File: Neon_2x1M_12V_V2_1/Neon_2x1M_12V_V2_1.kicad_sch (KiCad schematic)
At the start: 32 parts, among them J2 Barrel_Jack_MountingPin, J6 Conn_01x03_Pin, J7 Screw_Terminal_01x02, J8 Screw_Terminal_01x02, Q3 AO3400A, Q4 AO3400A, SW1 SW_Push, SW2 SW_Push, U1 ESP32-WROOM-32, U2 AMS1117-3.3

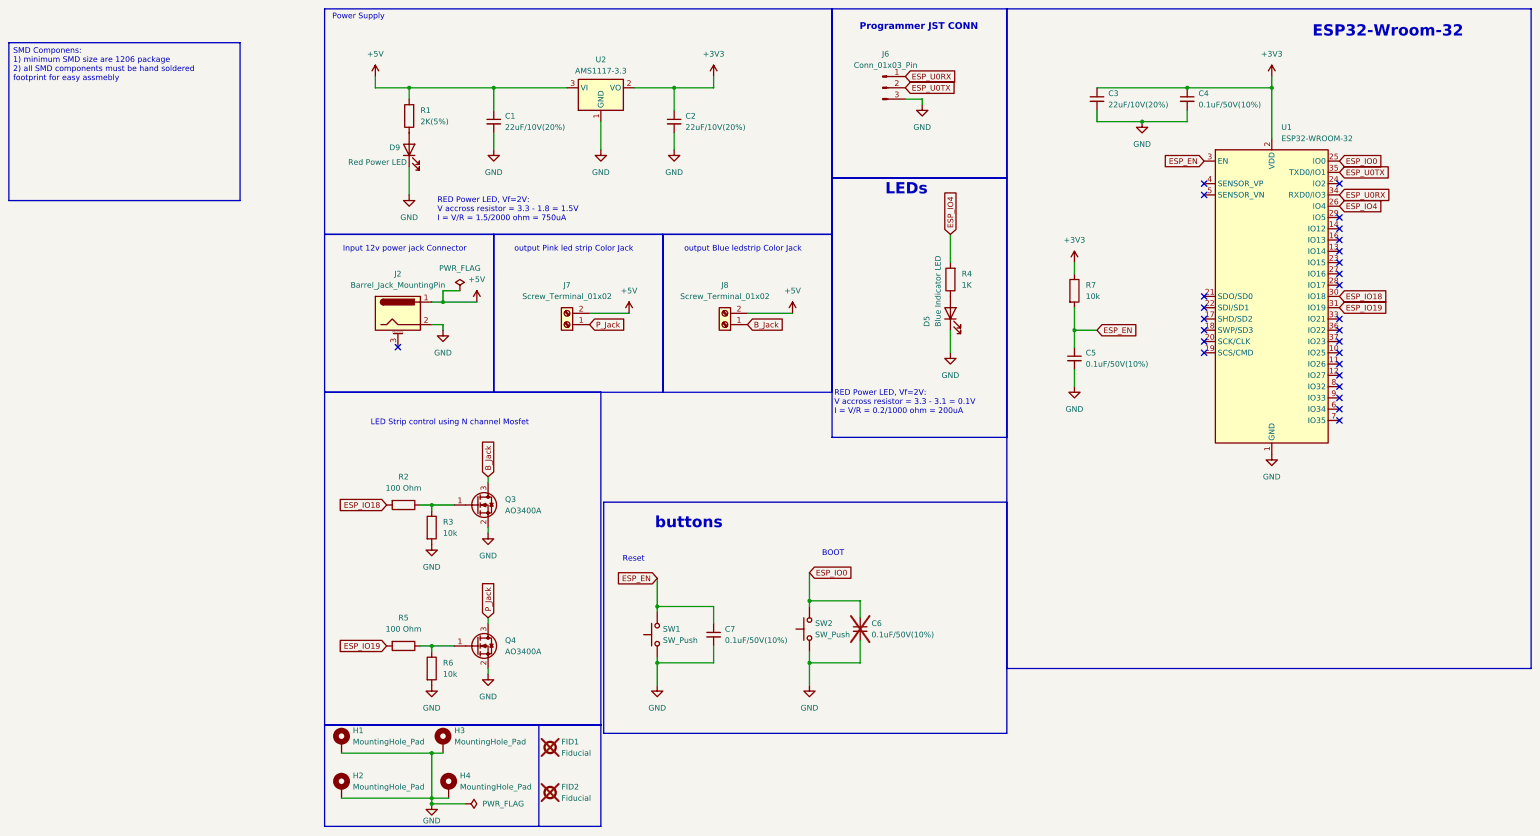
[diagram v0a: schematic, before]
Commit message: updated schematic and footprints
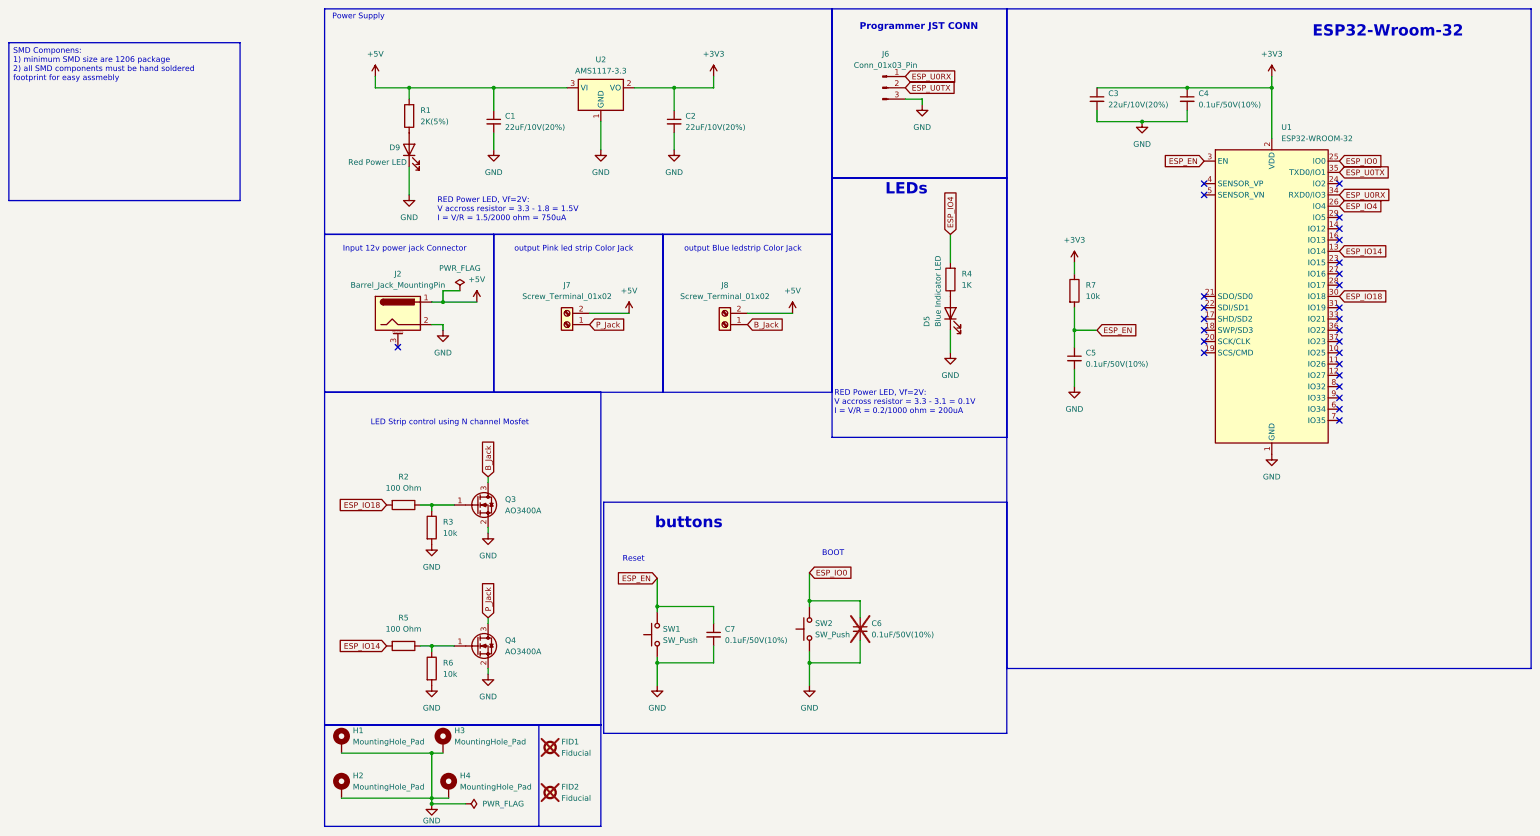
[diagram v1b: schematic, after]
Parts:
- C1, C2, C3, C4, C5, C6, C7: footprint (none) -> Capacitor_SMD:C_1206_3216Metric_Pad1.33x1.80mm_HandSolder
- Q3, Q4: footprint Package_TO_SOT_SMD:SOT-23 -> Package_TO_SOT_SMD:TSOT-23_HandSoldering
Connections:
- net ESP_IO14: now reaches U1.13 (IO14)
- net ESP_IO14: now also R5.2
- net ESP_IO19: no longer names the net of U1.31 (IO19)
- net ESP_IO19: no longer R5.2
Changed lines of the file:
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@@
 	)
 	(no_connect
-		(at 210.82 85.09)
+		(at 241.3 80.01)
 	)
 	(no_connect
-		(at 210.82 80.01)
+		(at 210.82 85.09)
 	)
 	(no_connect
-		(at 241.3 67.31)
+		(at 210.82 80.01)
 	)
 	(no_connect
@@
 		)
 	)
-	(global_label "ESP_IO19"
+	(global_label "ESP_IO14"
 		(shape input)
 		(at 26.67 156.21 180)
@@
 		)
 	)
-	(global_label "ESP_IO19"
-		(shape input)
-		(at 241.3 80.01 0)
-		(fields_autoplaced yes)
-		(effects
-			(font
-				(size 1.27 1.27)
-			)
-			(justify left)
-		)
-		(property "Intersheetrefs" "${INTERSHEET_REFS}"
-			(at 253.2356 80.01 0)
-			(hide yes)
-			(show_name no)
-			(do_not_autoplace no)
-			(effects
-				(font
-					(size 1.27 1.27)
-				)
-				(justify left)
-			)
-		)
-	)
 	(global_label "ESP_IO4"
 		(shape input)
@@
 		)
 	)
+	(global_label "ESP_IO14"
+		(shape input)
+		(at 241.3 67.31 0)
+		(fields_autoplaced yes)
+		(effects
+			(font
+				(size 1.27 1.27)
+			)
+			(justify left)
+		)
+		(property "Intersheetrefs" "${INTERSHEET_REFS}"
+			(at 253.2356 67.31 0)
+			(hide yes)
+			(show_name no)
+			(do_not_autoplace no)
+			(effects
+				(font
+					(size 1.27 1.27)
+				)
+				(justify left)
+			)
+		)
+	)
 	(global_label "P_Jack"
 		(shape input)
@@
 			)
 		)
-		(property "Footprint" ""
+		(property "Footprint" "Capacitor_SMD:C_1206_3216Metric_Pad1.33x1.80mm_HandSolder"
 			(at 50.8 38.1 0)
 			(hide yes)
@@
 			)
 		)
-		(property "Footprint" "Package_TO_SOT_SMD:SOT-23"
+		(property "Footprint" "Package_TO_SOT_SMD:TSOT-23_HandSoldering"
 			(at 52.07 126.365 0)
 			(hide yes)
@@
 			)
 		)
-		(property "Footprint" ""
+		(property "Footprint" "Capacitor_SMD:C_1206_3216Metric_Pad1.33x1.80mm_HandSolder"
 			(at 207.01 33.02 0)
 			(hide yes)
@@
 			)
 		)
-		(property "Footprint" "Package_TO_SOT_SMD:SOT-23"
+		(property "Footprint" "Package_TO_SOT_SMD:TSOT-23_HandSoldering"
 			(at 52.07 158.115 0)
 			(hide yes)
@@
 			)
 		)
-		(property "Footprint" ""
+		(property "Footprint" "Capacitor_SMD:C_1206_3216Metric_Pad1.33x1.80mm_HandSolder"
 			(at 91.44 38.1 0)
 			(hide yes)
@@
 			)
 		)
-		(property "Footprint" ""
+		(property "Footprint" "Capacitor_SMD:C_1206_3216Metric_Pad1.33x1.80mm_HandSolder"
 			(at 100.33 153.67 0)
 			(hide yes)
@@
 			)
 		)
-		(property "Footprint" ""
+		(property "Footprint" "Capacitor_SMD:C_1206_3216Metric_Pad1.33x1.80mm_HandSolder"
 			(at 186.69 33.02 0)
 			(hide yes)
@@
 			)
 		)
-		(property "Footprint" ""
+		(property "Footprint" "Capacitor_SMD:C_1206_3216Metric_Pad1.33x1.80mm_HandSolder"
 			(at 181.61 91.44 0)
 			(hide yes)
@@
 			)
 		)
-		(property "Footprint" ""
+		(property "Footprint" "Capacitor_SMD:C_1206_3216Metric_Pad1.33x1.80mm_HandSolder"
 			(at 133.35 152.4 0)
 			(hide yes)

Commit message: updated PCB layout
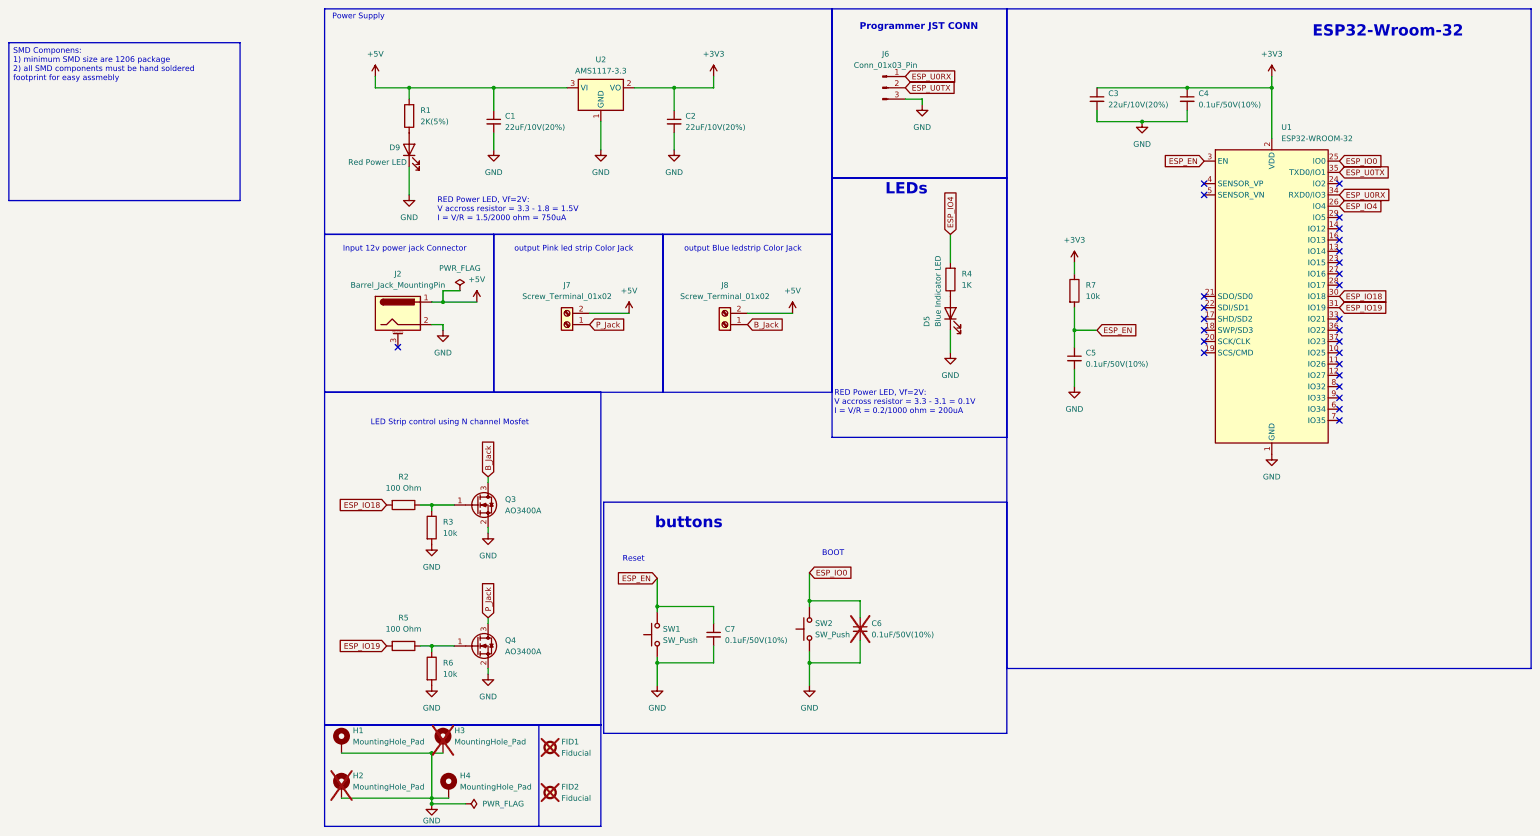
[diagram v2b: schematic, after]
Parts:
- H2, H3: now not fitted
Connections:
- net ESP_IO19: now reaches U1.31 (IO19)
- net ESP_IO19: now also R5.2
- net ESP_IO14: no longer names the net of U1.13 (IO14)
- net ESP_IO14: no longer R5.2
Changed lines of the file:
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@@
-	)
-	(no_connect
-		(at 241.3 80.01)
 	)
 	(no_connect
@@
 	)
 	(no_connect
+		(at 241.3 67.31)
+	)
+	(no_connect
 		(at 210.82 77.47)
 	)
@@
 		)
 	)
-	(global_label "ESP_IO14"
+	(global_label "ESP_IO19"
 		(shape input)
 		(at 26.67 156.21 180)
@@
 		)
 	)
+	(global_label "ESP_IO19"
+		(shape input)
+		(at 241.3 80.01 0)
+		(fields_autoplaced yes)
+		(effects
+			(font
+				(size 1.27 1.27)
+			)
+			(justify left)
+		)
+		(property "Intersheetrefs" "${INTERSHEET_REFS}"
+			(at 253.2356 80.01 0)
+			(hide yes)
+			(show_name no)
+			(do_not_autoplace no)
+			(effects
+				(font
+					(size 1.27 1.27)
+				)
+				(justify left)
+			)
+		)
+	)
 	(global_label "ESP_U0TX"
 		(shape input)
@@
 				)
 				(justify right)
-			)
-		)
-	)
-	(global_label "ESP_IO14"
-		(shape input)
-		(at 241.3 67.31 0)
-		(fields_autoplaced yes)
-		(effects
-			(font
-				(size 1.27 1.27)
-			)
-			(justify left)
-		)
-		(property "Intersheetrefs" "${INTERSHEET_REFS}"
-			(at 253.2356 67.31 0)
-			(hide yes)
-			(show_name no)
-			(do_not_autoplace no)
-			(effects
-				(font
-					(size 1.27 1.27)
-				)
-				(justify left)
 			)
 		)
@@
 		(exclude_from_sim no)
 		(in_bom no)
-		(on_board yes)
+		(on_board no)
 		(in_pos_files yes)
-		(dnp no)
+		(dnp yes)
 		(fields_autoplaced yes)
 		(property "Reference" "H3"
@@
 		(exclude_from_sim no)
 		(in_bom no)
-		(on_board yes)
+		(on_board no)
 		(in_pos_files yes)
-		(dnp no)
+		(dnp yes)
 		(fields_autoplaced yes)
 		(property "Reference" "H2"
